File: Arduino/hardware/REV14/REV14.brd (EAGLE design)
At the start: 49.5 x 49.5 mm, 23 parts, among them IC2 ATMEGA168-AU, Q1 32768Hz, U2 RFM95WSMD

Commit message: updated rev 14
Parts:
- removed ANT: ANT (86 mm), wirepad:2,15/1,0
- removed C11: 100nF, resistor:C0603
- removed C8: 100u, SparkFun-Passives:EIA3216
- removed R12, R5: 4.7K, resistor:R0603
- removed U2: RFM95WSMD, misiek:RFM95W_SMD
- added C5: 100nF, resistor:C0603
- added DQ: (no value), wirepad:2,15/1,0
- added R3: 4.7K, resistor:R0603
- added U1: RN2483, RFM95W-RN2483:RN2483
- I2C_EXT: device pinhead:2X07 -> pinhead:2X10
- moved C4 14.4 mm to (17.1, 23.5)
- moved I2C_EXT 3.81 mm to (3.81, 35.6)
- moved R9 2.84 mm to (12.7, 44.5)
- moved R4 2.62 mm to (12.7, 39.4), turned to 180 degrees
- renumbered PHT1 to PHT, U$4 to U4
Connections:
- removed net N$22: ANT.1, U2.9
- new net 3.3V: U1.12, U1.34
- new net RN2483_RESET: IC2.9
- new net RN2483_UART_RX: IC2.2
- new net RN2483_UART_TX: IC2.1
- net D2: now also DQ.1, I2C_EXT.17; no longer I2C_EXT.14
- net GND: now also I2C_EXT.10, I2C_EXT.12, U1.1, U1.11, U1.8; no longer C8.C, U2.1, U2.10, U2.8
- net IO_POWER_UP: now also I2C_EXT.19
- net N$1: now also I2C_EXT.18, R3.2; no longer C11.2, I2C_EXT.5
- net N$3: now also I2C_EXT.16, R4.2; no longer I2C_EXT.12, R5.2
- net N$4: now also C5.2, I2C_EXT.20; no longer I2C_EXT.11, R4.2
- net RESET: now also C5.1, I2C_EXT.5; no longer C11.1
- net RFM_IRQ: now also I2C_EXT.13; no longer I2C_EXT.7
- net RX: now also R3.1; no longer R4.1
- net SDA: now also I2C_EXT.11; no longer I2C_EXT.10
- net SPI_MISO: no longer U2.2
- net SPI_MOSI: no longer U2.3
- net SPI_NSS: now also I2C_EXT.15; no longer I2C_EXT.8, R12.1, U2.5
- net SPI_SCK: no longer U2.4
- net TX: now also R4.1; no longer R5.1
- net VCC: no longer C8.A, R12.2, U2.13
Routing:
- net VCC: track 159.0 -> 0.00 mm
- net SDA: track 113.0 -> 0.00 mm, vias 3 -> 0
- net SCL: track 110.6 -> 0.00 mm, vias 2 -> 0
- net SPI_SCK: track 69.8 -> 0.00 mm, vias 1 -> 0
- net SPI_NSS: track 69.7 -> 0.00 mm, vias 4 -> 0
- net SPI_MOSI: track 66.2 -> 0.00 mm
- net SPI_MISO: track 53.3 -> 0.00 mm
- net RESET: track 50.4 -> 0.00 mm, vias 2 -> 0
- net RFM_IRQ: track 40.0 -> 0.00 mm, vias 2 -> 0
- net D2: track 34.0 -> 0.00 mm, vias 2 -> 0
- net TX: track 25.7 -> 0.00 mm, vias 2 -> 0
- net RX: track 25.5 -> 0.00 mm, vias 2 -> 0
- net LDR: track 17.5 -> 0.00 mm
- net IO_POWER_UP: track 15.7 -> 0.00 mm, vias 1 -> 0
- net GND: track 15.6 -> 0.00 mm, vias 9 -> 0
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
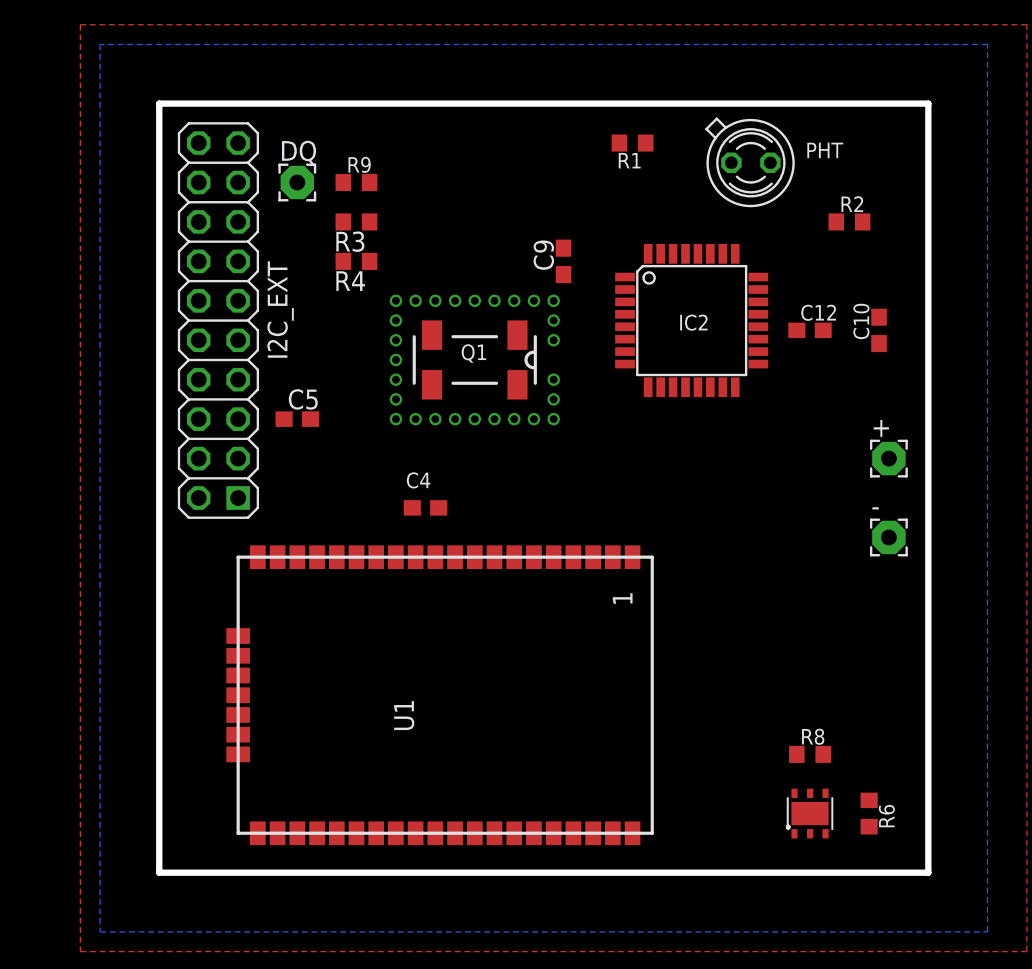
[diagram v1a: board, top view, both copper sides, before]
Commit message: rev 14 ant tracks and xtal done
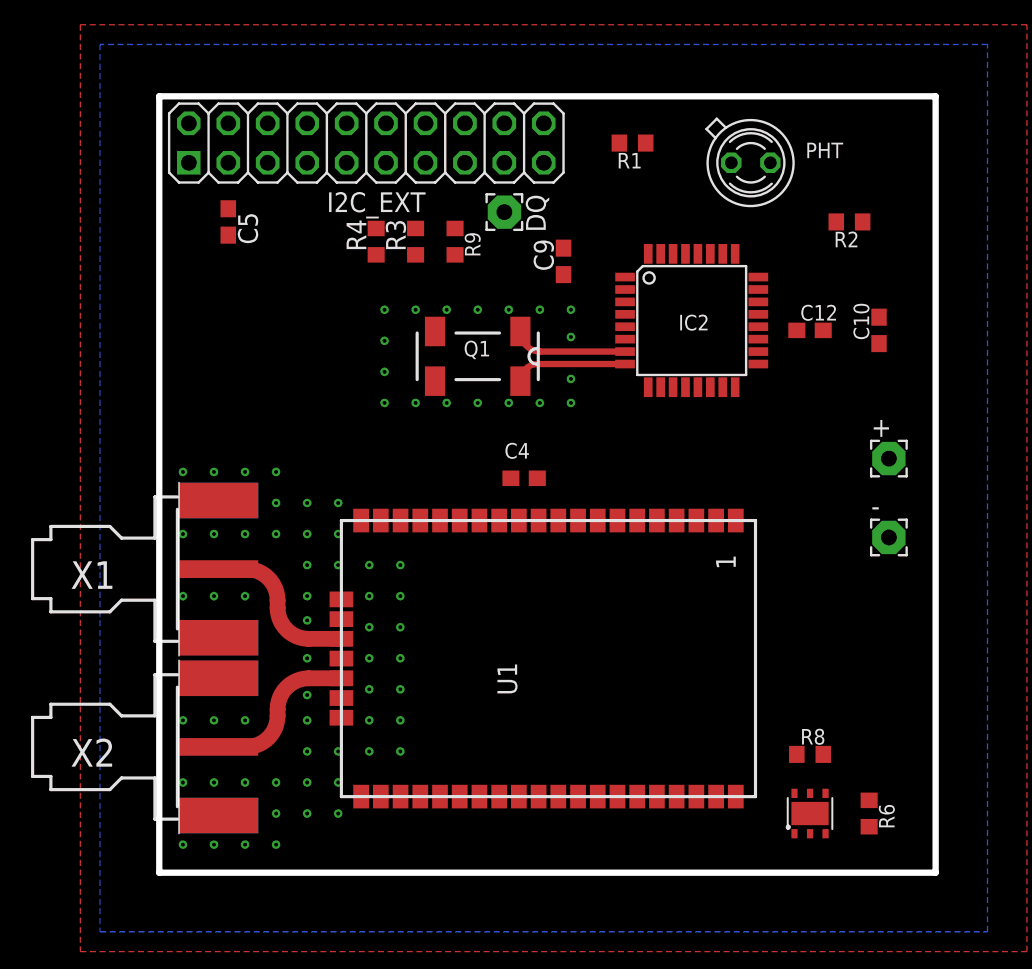
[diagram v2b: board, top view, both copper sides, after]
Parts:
- added X1, X2: SMA-142-0701-881/886, con-coax:J502-ND-142-0701-881/886
- moved I2C_EXT 14.9 mm to (13.3, 47.0), turned to 0 degrees
- moved DQ 13.5 mm to (22.2, 42.5), turned to 270 degrees
- moved C5 13.5 mm to (4.45, 41.9), turned to 270 degrees
- moved R9 7.41 mm to (19.1, 40.6), turned to 270 degrees
- moved U1 7.06 mm to (38.4, 4.90)
- moved C4 6.63 mm to (23.5, 25.4)
- moved R3 4.02 mm to (16.5, 40.6), turned to 90 degrees
- moved R4 1.80 mm to (14.0, 40.6), turned to 90 degrees
- moved Q1 0.30 mm to (20.5, 33.3)
- turned R2 to 180 degrees
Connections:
- removed net 3.3V: U1.12, U1.34
- new net N$22: U1.23, X1.1
- new net N$33: U1.25, X2.1
- new net RN2483_UART_CTS: IC2.10, U1.3
- new net RN2483_UART_RTS: U1.2
- net GND: now also U1.20, U1.21, U1.22, U1.24, U1.26, U1.27, U1.28, U1.33, U1.41, U1.47, X1.G@1, X1.G@2, X1.G@3, X1.G@4, X2.G@1, X2.G@2, X2.G@3, X2.G@4
- net RN2483_RESET: now also U1.32
- net RN2483_UART_RX: now also U1.7
- net RN2483_UART_TX: now also U1.6
- net VCC: now also U1.12, U1.34
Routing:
- net N$22: track 0.00 -> 10.0 mm
- net N$33: track 0.00 -> 9.97 mm
- net XTAL2: track 0.00 -> 7.27 mm
- net XTAL1: track 0.00 -> 7.20 mm
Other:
- board size 49.5 x 49.5 mm -> 50 x 50 mm

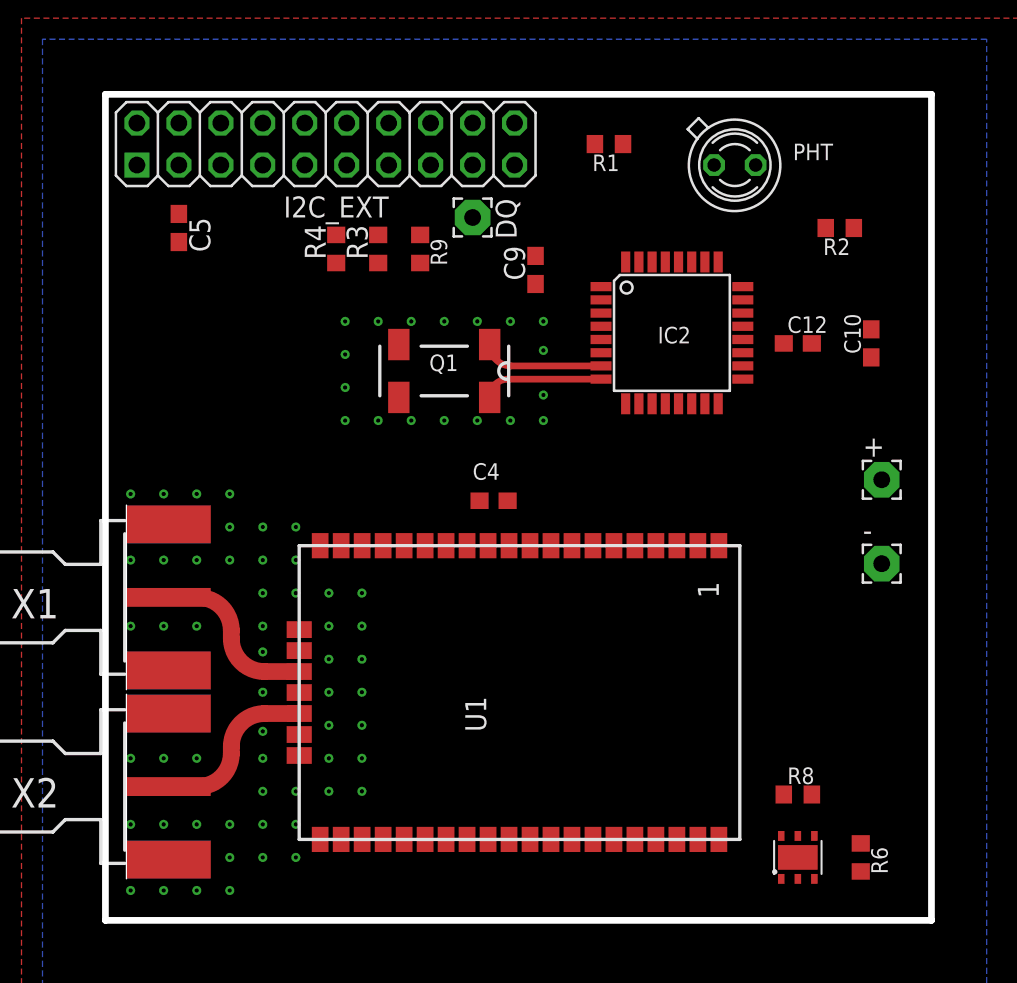
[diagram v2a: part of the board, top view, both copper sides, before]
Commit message: rev14 ready for routing
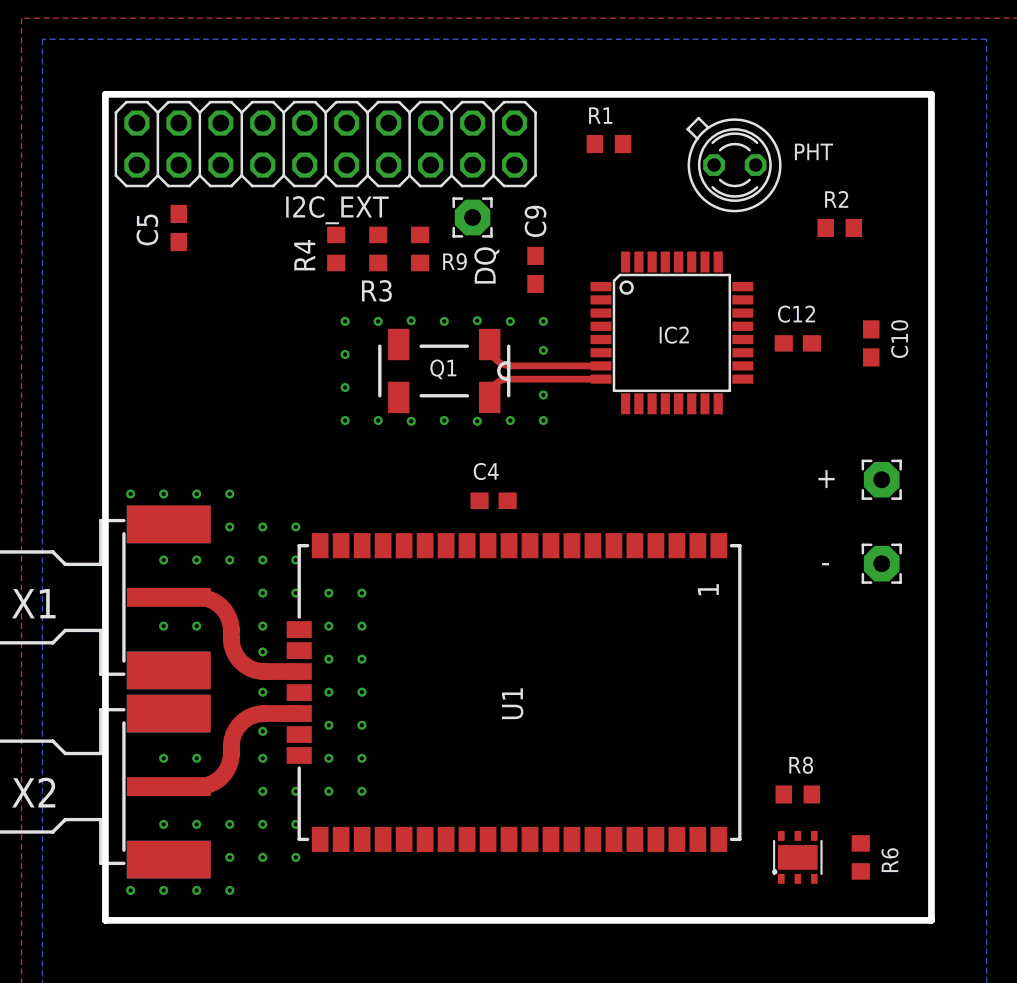
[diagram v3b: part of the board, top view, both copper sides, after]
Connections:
- net RN2483_UART_RTS: now also IC2.11
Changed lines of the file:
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@@
 </element>
 <element name="C9" library="resistor" package="C0603" value="100nF" x="26.035" y="39.37" smashed="yes" rot="R90">
-<attribute name="NAME" x="25.4" y="38.735" size="1.27" layer="25" rot="R90"/>
+<attribute name="NAME" x="26.67" y="41.275" size="1.27" layer="25" rot="R90"/>
 </element>
 <element name="C10" library="resistor" package="C0603" value="100nF" x="46.355" y="34.925" smashed="yes" rot="R90">
-<attribute name="NAME" x="45.72" y="34.29" size="1" layer="25" rot="R90"/>
+<attribute name="NAME" x="48.5775" y="33.9725" size="1" layer="25" rot="R90"/>
 </element>
 <element name="C12" library="resistor" package="C0603" value="100nF" x="41.91" y="34.925" smashed="yes">
-<attribute name="NAME" x="41.275" y="35.56" size="1" layer="25"/>
+<attribute name="NAME" x="40.64" y="36.195" size="1" layer="25"/>
 </element>
 <element name="IC2" library="Arduino-AVR" package="TQFP32-08" value="ATMEGA168-AU" x="34.29" y="35.56" smashed="yes">
@@
 </element>
 <element name="R6" library="resistor" package="R0603" value="4.7K" x="45.72" y="3.81" smashed="yes" rot="R270">
-<attribute name="NAME" x="46.355" y="4.445" size="1" layer="25" rot="R270"/>
+<attribute name="NAME" x="46.99" y="4.445" size="1" layer="25" rot="R270"/>
 </element>
 <element name="R8" library="resistor" package="R0603" value="4.7K" x="41.91" y="7.62" smashed="yes">
-<attribute name="NAME" x="41.275" y="8.255" size="1" layer="25"/>
+<attribute name="NAME" x="41.275" y="8.89" size="1" layer="25"/>
 </element>
 <element name="U4" library="SHT21" package="SHT21" value="SHT21" x="41.91" y="3.81"/>
 <element name="R1" library="resistor" package="R0603" value="100K" x="30.48" y="46.99" smashed="yes" rot="R180">
-<attribute name="NAME" x="31.115" y="46.355" size="1" layer="25" rot="R180"/>
+<attribute name="NAME" x="30.7975" y="49.2125" size="1" layer="25" rot="R180"/>
 </element>
 <element name="PHT" library="opto-trans-siemens" package="BPX65" value="BPX65" x="38.1" y="45.72" smashed="yes" rot="R315">
@@
 </element>
 <element name="R9" library="resistor" package="R0603" value="4.7K" x="19.05" y="40.64" smashed="yes" rot="R270">
-<attribute name="NAME" x="19.685" y="41.275" size="1" layer="25" rot="R270"/>
+<attribute name="NAME" x="20.32" y="39.37" size="1" layer="25"/>
 </element>
 <element name="Q1" library="crystal" package="MC-306" value="32768Hz" x="20.51" y="33.255" smashed="yes" rot="R180">
@@
 <attribute name="MF" value="" x="30.67" y="21.825" size="1.778" layer="27" rot="R180" display="off"/>
 <attribute name="MPN" value="MC-306 60.0KHZ  100PPM ,12.5PF" x="30.67" y="21.825" size="1.778" layer="27" rot="R180" display="off"/>
-<attribute name="NAME" x="21.3542" y="34.25" size="1" layer="25" rot="R180"/>
+<attribute name="NAME" x="21.3542" y="33.9325" size="1" layer="25" rot="R180"/>
 </element>
 <element name="R2" library="resistor" package="R0603" value="4.7K" x="44.45" y="41.91" smashed="yes" rot="R180">
-<attribute name="NAME" x="45.085" y="41.275" size="1" layer="25" rot="R180"/>
-</element>
-<element name="-" library="wirepad" package="2,15/1,0" value="" x="46.99" y="21.59"/>
-<element name="+" library="wirepad" package="2,15/1,0" value="" x="46.99" y="26.67"/>
+<attribute name="NAME" x="45.085" y="44.1325" size="1" layer="25" rot="R180"/>
+</element>
+<element name="-" library="wirepad" package="2,15/1,0" value="" x="46.99" y="21.59" smashed="yes">
+<attribute name="NAME" x="43.307" y="21.082" size="1.27" layer="25" ratio="10"/>
+<attribute name="VALUE" x="46.99" y="22.59" size="0.0254" layer="27"/>
+</element>
+<element name="+" library="wirepad" package="2,15/1,0" value="" x="46.99" y="26.67" smashed="yes">
+<attribute name="NAME" x="42.9895" y="26.162" size="1.27" layer="25" ratio="10"/>
+<attribute name="VALUE" x="46.99" y="27.67" size="0.0254" layer="27"/>
+</element>
 <element name="U1" library="RFM95W-RN2483" package="RN2483" value="RN2483" x="38.4" y="4.9" smashed="yes" rot="R90">
-<attribute name="NAME" x="23.05" y="11.41" size="1.27" layer="25" rot="R90"/>
+<attribute name="NAME" x="25.2725" y="12.045" size="1.27" layer="25" rot="R90"/>
 </element>
 <element name="I2C_EXT" library="pinhead" package="2X10" value="" x="13.335" y="46.99" smashed="yes">
@@
 <attribute name="VALUE" x="0.635" y="42.545" size="1.27" layer="27"/>
 </element>
-<element name="DQ" library="wirepad" package="2,15/1,0" value="" x="22.225" y="42.545" rot="R270"/>
+<element name="DQ" library="wirepad" package="2,15/1,0" value="" x="22.225" y="42.545" smashed="yes" rot="R270">
+<attribute name="NAME" x="22.352" y="40.8305" size="1.27" layer="25" ratio="10" rot="R270"/>
+<attribute name="VALUE" x="23.225" y="42.545" size="0.0254" layer="27" rot="R270"/>
+</element>
 <element name="R3" library="resistor" package="R0603" value="4.7K" x="16.51" y="40.64" smashed="yes" rot="R90">
-<attribute name="NAME" x="15.875" y="40.005" size="1.27" layer="25" rot="R90"/>
+<attribute name="NAME" x="17.4625" y="38.735" size="1.27" layer="25" rot="R180"/>
 </element>
 <element name="R4" library="resistor" package="R0603" value="4.7K" x="13.97" y="40.64" smashed="yes" rot="R90">
-<attribute name="NAME" x="13.335" y="40.005" size="1.27" layer="25" rot="R90"/>
+<attribute name="NAME" x="11.43" y="41.275" size="1.27" layer="25" rot="R270"/>
 </element>
 <element name="C5" library="resistor" package="C0603" value="100nF" x="4.445" y="41.91" smashed="yes" rot="R270">
-<attribute name="NAME" x="5.08" y="42.545" size="1.27" layer="25" rot="R270"/>
+<attribute name="NAME" x="1.905" y="42.8625" size="1.27" layer="25" rot="R270"/>
 </element>
 <element name="X1" library="con-coax" package="J502-ND-142-0701-881/886" value="SMA-142-0701-881/886" x="1.27" y="19.55" smashed="yes">
@@
 <via x="5.525" y="5.81" extent="1-16" drill="0.25"/>
 <via x="3.525" y="5.81" extent="1-16" drill="0.25"/>
-<via x="1.525" y="5.81" extent="1-16" drill="0.25"/>
-<via x="1.525" y="9.81" extent="1-16" drill="0.25"/>
+<wire x1="1.525" y1="5.81" x2="1.525" y2="5.81" width="0" layer="19" extent="1-16"/>
+<wire x1="1.525" y1="9.81" x2="1.525" y2="9.81" width="0" layer="19" extent="1-16"/>
 <via x="3.525" y="9.81" extent="1-16" drill="0.25"/>
 <via x="5.525" y="9.81" extent="1-16" drill="0.25"/>
@@
 <via x="5.525" y="17.81" extent="1-16" drill="0.25"/>
 <via x="3.525" y="17.81" extent="1-16" drill="0.25"/>
-<via x="1.525" y="17.81" extent="1-16" drill="0.25"/>
+<wire x1="1.525" y1="17.81" x2="1.525" y2="17.81" width="0" layer="19" extent="1-16"/>
 <via x="5.525" y="21.81" extent="1-16" drill="0.25"/>
 <via x="3.525" y="21.81" extent="1-16" drill="0.25"/>
-<via x="1.525" y="21.81" extent="1-16" drill="0.25"/>
+<wire x1="1.525" y1="21.81" x2="1.525" y2="21.81" width="0" layer="19" extent="1-16"/>
 <via x="11.525" y="19.81" extent="1-16" drill="0.25"/>
 <via x="11.525" y="21.81" extent="1-16" drill="0.25"/>
@@
 <via x="26.51" y="36.255" extent="1-16" drill="0.25"/>
 <via x="26.51" y="34.5" extent="1-16" drill="0.25"/>
-<via x="22.51" y="30.255" extent="1-16" drill="0.25"/>
+<via x="22.51" y="30.21" extent="1-16" drill="0.25"/>
 <via x="20.51" y="30.255" extent="1-16" drill="0.25"/>
 <via x="16.51" y="30.255" extent="1-16" drill="0.25"/>
-<via x="18.51" y="30.255" extent="1-16" drill="0.25"/>
+<via x="18.51" y="30.21" extent="1-16" drill="0.25"/>
 <via x="24.51" y="30.255" extent="1-16" drill="0.25"/>
-<via x="22.51" y="36.255" extent="1-16" drill="0.25"/>
+<via x="22.51" y="36.3" extent="1-16" drill="0.25"/>
 <via x="20.51" y="36.255" extent="1-16" drill="0.25"/>
 <via x="16.51" y="36.255" extent="1-16" drill="0.25"/>
-<via x="18.51" y="36.255" extent="1-16" drill="0.25"/>
+<via x="18.51" y="36.3" extent="1-16" drill="0.25"/>
 <via x="24.51" y="36.255" extent="1-16" drill="0.25"/>
 <contactref element="U1" pad="28"/>
@@
 <signal name="RN2483_UART_RTS">
 <contactref element="U1" pad="2"/>
+<contactref element="IC2" pad="11"/>
+<wire x1="35.86" y1="22.68" x2="33.09" y2="31.2674" width="0" layer="19" extent="1-1"/>
 </signal>
 <signal name="N$22" class="2">
